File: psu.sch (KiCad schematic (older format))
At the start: 19 parts, among them J5 Screw_Terminal_01x03, U13 L7812, U14 L7912

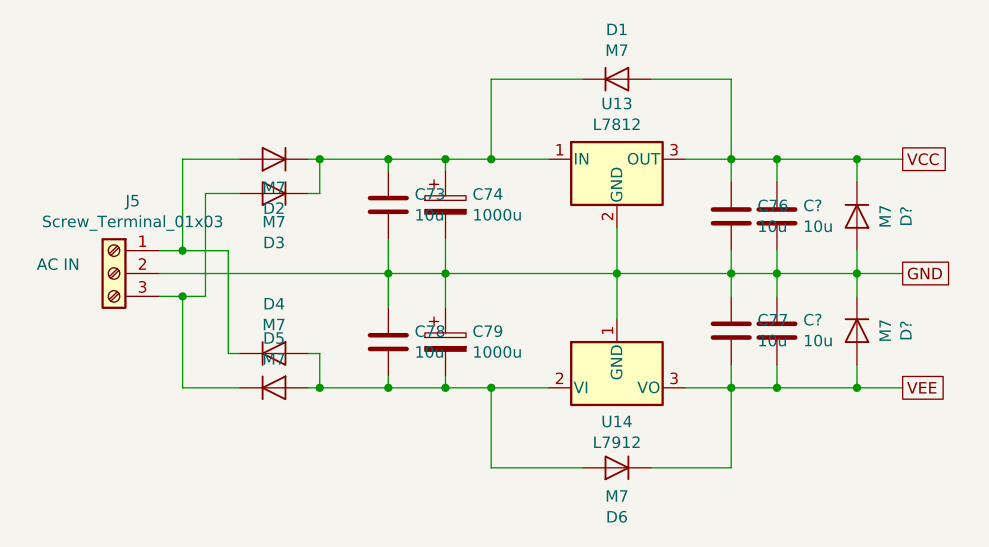
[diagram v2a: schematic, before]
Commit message: added buffered volume pot, and fixed subsonic filter added signal taps for external transforms/filters to be added later
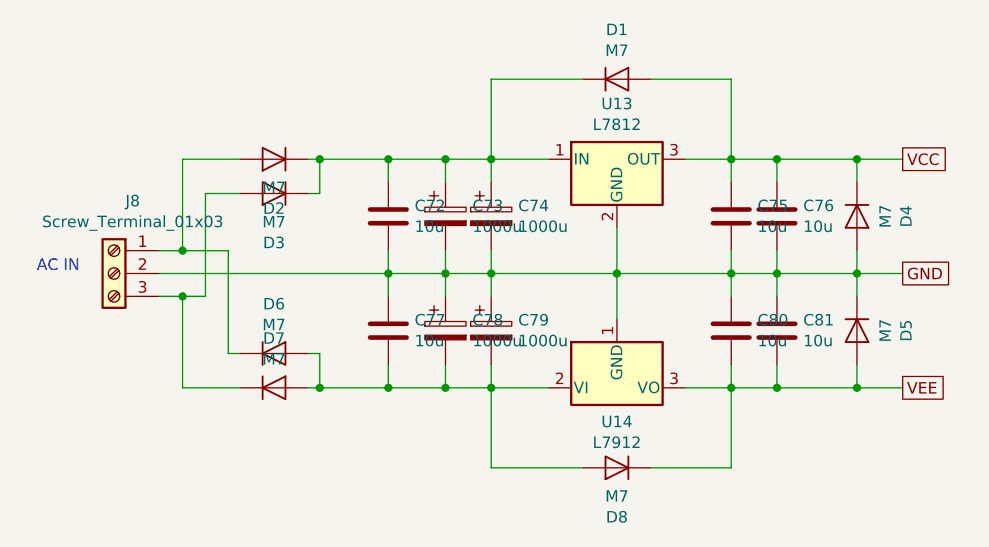
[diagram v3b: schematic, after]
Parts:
- added C74, C79: 1000u, Capacitors_ThroughHole:CP_Radial_D16.0mm_P7.50mm, symbol Device:CP
- gave numbers to parts that had none: 4
- renumbered C73 to C72, C74 to C73, C76 to C75, C78 to C77, C79 to C78, C77 to C80, D4 to D6, D5 to D7, D6 to D8, J5 to J8
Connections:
- net GND: now also C74.2, C79.1
- net at C72.1, C73.1, D1.1 (K)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: now also C74.1
- net at C77.2, C78.2, D6.2 (A)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: now also C79.2
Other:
- moved on the sheet: C72, C73, C77, C78
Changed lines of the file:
@@
 $Descr A4 11693 8268
 encoding utf-8
-Sheet 13 13
+Sheet 12 19
 Title "Linear Power Supply for Crossovers"
 Date "2021-10-03"
@@
 $EndDescr
 $Comp
-L Connector:Screw_Terminal_01x03 J5
+L Connector:Screw_Terminal_01x03 J8
 U 1 1 61A2D78B
 P 2400 2200
-F 0 "J5" H 2318 2517 50  0000 C CNN
+F 0 "J8" H 2318 2517 50  0000 C CNN
 F 1 "Screw_Terminal_01x03" H 2318 2426 50  0000 C CNN
 F 2 "Terminals_Phoenix:TerminalBlock_Phoenix_MKDS1.5-3pol" H 2400 2200 50  0001 C CNN
@@
 AC IN
 $Comp
-L Device:CP C74
+L Device:CP C73
 U 1 1 61A39623
-P 3850 1900
-F 0 "C74" H 3968 1946 50  0000 L CNN
-F 1 "1000u" H 3968 1855 50  0000 L CNN
-F 2 "Capacitors_ThroughHole:CP_Radial_D16.0mm_P7.50mm" H 3888 1750 50  0001 C CNN
-F 3 "~" H 3850 1900 50  0001 C CNN
-	1    3850 1900
-	1    0    0    -1
-$EndComp
-$Comp
-L Device:CP C79
+P 3850 1950
+F 0 "C73" H 3968 1996 50  0000 L CNN
+F 1 "1000u" H 3968 1905 50  0000 L CNN
+F 2 "Capacitors_ThroughHole:CP_Radial_D16.0mm_P7.50mm" H 3888 1800 50  0001 C CNN
+F 3 "~" H 3850 1950 50  0001 C CNN
+	1    3850 1950
+	1    0    0    -1
+$EndComp
+$Comp
+L Device:CP C78
 U 1 1 61A3D77A
-P 3850 2500
-F 0 "C79" H 3968 2546 50  0000 L CNN
-F 1 "1000u" H 3968 2455 50  0000 L CNN
-F 2 "Capacitors_ThroughHole:CP_Radial_D16.0mm_P7.50mm" H 3888 2350 50  0001 C CNN
-F 3 "~" H 3850 2500 50  0001 C CNN
-	1    3850 2500
-	1    0    0    -1
-$EndComp
-Wire Wire Line
-	3850 2050 3850 2200
-Connection ~ 3850 2200
-Wire Wire Line
-	3850 2200 3850 2350
-Wire Wire Line
-	3850 1700 3850 1750
+P 3850 2450
+F 0 "C78" H 3968 2496 50  0000 L CNN
+F 1 "1000u" H 3968 2405 50  0000 L CNN
+F 2 "Capacitors_ThroughHole:CP_Radial_D16.0mm_P7.50mm" H 3888 2300 50  0001 C CNN
+F 3 "~" H 3850 2450 50  0001 C CNN
+	1    3850 2450
+	1    0    0    -1
+$EndComp
 Wire Wire Line
 	3850 1700 4050 1700
@@
 Wire Wire Line
 	4050 2700 4300 2700
-Wire Wire Line
-	3850 2650 3850 2700
 Wire Wire Line
 	3850 2700 4050 2700
@@
 	4900 2700 5100 2700
 $Comp
-L Device:C C76
+L Device:C C75
 U 1 1 61A4AEE8
 P 5100 1950
-F 0 "C76" H 5215 1996 50  0000 L CNN
+F 0 "C75" H 5215 1996 50  0000 L CNN
 F 1 "10u" H 5215 1905 50  0000 L CNN
 F 2 "Capacitors_SMD:C_0805" H 5138 1800 50  0001 C CNN
@@
 	5100 2200 5300 2200
 $Comp
-L Device:C C77
+L Device:C C80
 U 1 1 61A4C047
 P 5100 2450
-F 0 "C77" H 5215 2496 50  0000 L CNN
+F 0 "C80" H 5215 2496 50  0000 L CNN
 F 1 "10u" H 5215 2405 50  0000 L CNN
 F 2 "Capacitors_SMD:C_0805" H 5138 2300 50  0001 C CNN
@@
 $EndComp
 $Comp
-L Device:D D6
+L Device:D D8
 U 1 1 61A561AB
 P 4600 3050
-F 0 "D6" H 4600 3266 50  0000 C CNN
+F 0 "D8" H 4600 3266 50  0000 C CNN
 F 1 "M7" H 4600 3175 50  0000 C CNN
 F 2 "Diodes_SMD:D_SMA" H 4600 3050 50  0001 C CNN
@@
 $EndComp
 $Comp
-L Device:D D5
+L Device:D D7
 U 1 1 61A5C8F9
 P 3100 2700
-F 0 "D5" H 3100 2916 50  0000 C CNN
+F 0 "D7" H 3100 2916 50  0000 C CNN
 F 1 "M7" H 3100 2825 50  0000 C CNN
 F 2 "Diodes_SMD:D_SMA" H 3100 2700 50  0001 C CNN
@@
 $EndComp
 $Comp
-L Device:D D4
+L Device:D D6
 U 1 1 61A5D636
 P 3100 2550
-F 0 "D4" H 3100 2766 50  0000 C CNN
+F 0 "D6" H 3100 2766 50  0000 C CNN
 F 1 "M7" H 3100 2675 50  0000 C CNN
 F 2 "Diodes_SMD:D_SMA" H 3100 2550 50  0001 C CNN
@@
 Connection ~ 3850 2700
 Wire Wire Line
-	2600 2200 3600 2200
-Wire Wire Line
 	3250 1700 3300 1700
 Wire Wire Line
@@
 Connection ~ 2700 2300
 $Comp
-L Device:C C73
+L Device:C C72
 U 1 1 615DA40F
-P 3600 1900
-F 0 "C73" H 3715 1946 50  0000 L CNN
-F 1 "10u" H 3715 1855 50  0000 L CNN
-F 2 "Capacitors_SMD:C_0805" H 3638 1750 50  0001 C CNN
-F 3 "~" H 3600 1900 50  0001 C CNN
-	1    3600 1900
-	1    0    0    -1
-$EndComp
-$Comp
-L Device:C C78
+P 3600 1950
+F 0 "C72" H 3715 1996 50  0000 L CNN
+F 1 "10u" H 3715 1905 50  0000 L CNN
+F 2 "Capacitors_SMD:C_0805" H 3638 1800 50  0001 C CNN
+F 3 "~" H 3600 1950 50  0001 C CNN
+	1    3600 1950
+	1    0    0    -1
+$EndComp
+$Comp
+L Device:C C77
 U 1 1 615DA6FF
-P 3600 2500
-F 0 "C78" H 3715 2546 50  0000 L CNN
-F 1 "10u" H 3715 2455 50  0000 L CNN
-F 2 "Capacitors_SMD:C_0805" H 3638 2350 50  0001 C CNN
-F 3 "~" H 3600 2500 50  0001 C CNN
-	1    3600 2500
-	1    0    0    -1
-$EndComp
-Wire Wire Line
-	3600 2700 3600 2650
+P 3600 2450
+F 0 "C77" H 3715 2496 50  0000 L CNN
+F 1 "10u" H 3715 2405 50  0000 L CNN
+F 2 "Capacitors_SMD:C_0805" H 3638 2300 50  0001 C CNN
+F 3 "~" H 3600 2450 50  0001 C CNN
+	1    3600 2450
+	1    0    0    -1
+$EndComp
 Connection ~ 3600 2700
 Wire Wire Line
 	3600 2700 3850 2700
-Wire Wire Line
-	3600 2350 3600 2200
-Connection ~ 3600 2200
-Wire Wire Line
-	3600 2200 3850 2200
-Wire Wire Line
-	3600 2200 3600 2050
-Wire Wire Line
-	3600 1750 3600 1700
 Connection ~ 3600 1700
 Wire Wire Line
 	3600 1700 3850 1700
 $Comp
-L Device:C C?
+L Device:C C76
 U 1 1 615FF89D
 P 5300 1950
-F 0 "C?" H 5415 1996 50  0000 L CNN
+F 0 "C76" H 5415 1996 50  0000 L CNN
 F 1 "10u" H 5415 1905 50  0000 L CNN
 F 2 "Capacitors_SMD:C_0805" H 5338 1800 50  0001 C CNN
@@
 $EndComp
 $Comp
-L Device:C C?
+L Device:C C81
 U 1 1 615FFB71
 P 5300 2450
-F 0 "C?" H 5415 2496 50  0000 L CNN
+F 0 "C81" H 5415 2496 50  0000 L CNN
 F 1 "10u" H 5415 2405 50  0000 L CNN
 F 2 "Capacitors_SMD:C_0805" H 5338 2300 50  0001 C CNN
@@
 Wire Wire Line
 	5300 2600 5300 2700
-Wire Wire Line
-	3850 2200 4600 2200
-$Comp
-L Device:D D?
+$Comp
+L Device:D D4
 U 1 1 61608971
 P 5650 1950
-F 0 "D?" H 5650 2166 50  0000 C CNN
+F 0 "D4" H 5650 2166 50  0000 C CNN
 F 1 "M7" H 5650 2075 50  0000 C CNN
 F 2 "Diodes_SMD:D_SMA" H 5650 1950 50  0001 C CNN
@@
 $EndComp
 $Comp
-L Device:D D?
+L Device:D D5
 U 1 1 6160A269
 P 5650 2450
-F 0 "D?" H 5650 2666 50  0000 C CNN
+F 0 "D5" H 5650 2666 50  0000 C CNN
 F 1 "M7" H 5650 2575 50  0000 C CNN
 F 2 "Diodes_SMD:D_SMA" H 5650 2450 50  0001 C CNN
@@
 Wire Wire Line
 	5650 2700 5850 2700
+$Comp
+L Device:CP C79
+U 1 1 61AA4FE6
+P 4050 2450
+F 0 "C79" H 4168 2496 50  0000 L CNN
+F 1 "1000u" H 4168 2405 50  0000 L CNN
+F 2 "Capacitors_ThroughHole:CP_Radial_D16.0mm_P7.50mm" H 4088 2300 50  0001 C CNN
+F 3 "~" H 4050 2450 50  0001 C CNN
+	1    4050 2450
+	1    0    0    -1
+$EndComp
+Wire Wire Line
+	2600 2200 3600 2200
+$Comp
+L Device:CP C74
+U 1 1 61AAA68E
+P 4050 1950
+F 0 "C74" H 4168 1996 50  0000 L CNN
+F 1 "1000u" H 4168 1905 50  0000 L CNN
+F 2 "Capacitors_ThroughHole:CP_Radial_D16.0mm_P7.50mm" H 4088 1800 50  0001 C CNN
+F 3 "~" H 4050 1950 50  0001 C CNN
+	1    4050 1950
+	1    0    0    -1
+$EndComp
+Wire Wire Line
+	4050 1700 4050 1800
+Wire Wire Line
+	3850 1700 3850 1800
+Wire Wire Line
+	3600 1700 3600 1800
+Wire Wire Line
+	3600 2100 3600 2200
+Connection ~ 3600 2200
+Wire Wire Line
+	3600 2200 3850 2200
+Wire Wire Line
+	3600 2200 3600 2300
+Wire Wire Line
+	3600 2600 3600 2700
+Wire Wire Line
+	3850 2600 3850 2700
+Wire Wire Line
+	3850 2100 3850 2200
+Connection ~ 3850 2200
+Wire Wire Line
+	3850 2200 4050 2200
+Wire Wire Line
+	4050 2300 4050 2200
+Connection ~ 4050 2200
+Wire Wire Line
+	4050 2200 4600 2200
+Wire Wire Line
+	4050 2200 4050 2100
+Wire Wire Line
+	3850 2200 3850 2300
+Wire Wire Line
+	4050 2600 4050 2700
 $EndSCHEMATC

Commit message: inverted LF processing chain, now with BW2 subsonic filter
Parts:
- added J?: Screw_Terminal_01x02, Terminals_Phoenix:TerminalBlock_Phoenix_MPT-2.54mm_2pol, symbol Connector:Screw_Terminal_01x02
- added J?: Screw_Terminal_01x03, Terminals_Phoenix:TerminalBlock_Phoenix_MKDS1.5-3pol, symbol Connector:Screw_Terminal_01x03
- added JP?: Jumper_2_Bridged, symbol Jumper:Jumper_2_Bridged
- added JP? (x2): Jumper_2_Open, symbol Jumper:Jumper_2_Open
- added TR?: TRANSF6, symbol Transformer:TRANSF6
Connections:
- wire segments 76 -> 125
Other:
- note added: "115/230 jumpers"
- note added: "DC"
- note added: "HV AC"
- note added: "LV AC"
- note removed: "AC IN"
- moved on the sheet: C72, C73, C74, C75, C76, C77, C78, C79, C80, C81, D1, D2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
